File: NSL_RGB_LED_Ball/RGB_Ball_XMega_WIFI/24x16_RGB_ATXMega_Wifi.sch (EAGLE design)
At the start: 105 parts, among them IC2 TLC5947XLP, IC3 TLC5947XLP, IC4 TLC5947XLP, IC5 MCP73123, IC6 CC3000, IC7 MMA7455L, IC8 OPA344, X1 NX3225GA XC1972CT-ND

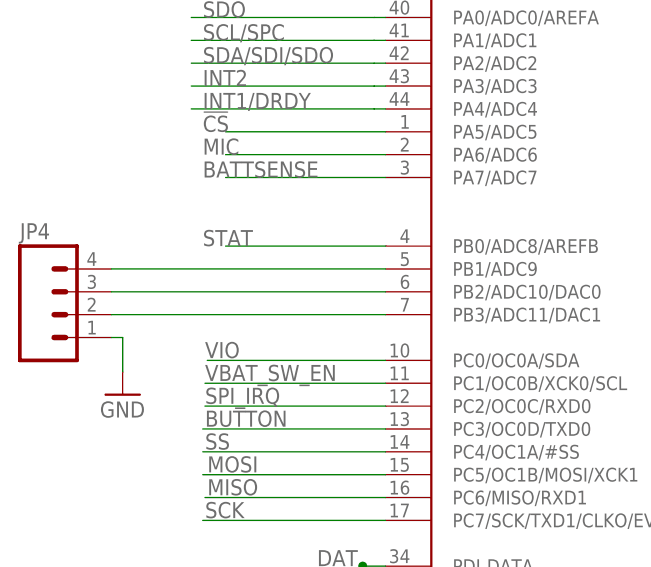
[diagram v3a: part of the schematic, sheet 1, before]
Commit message: 
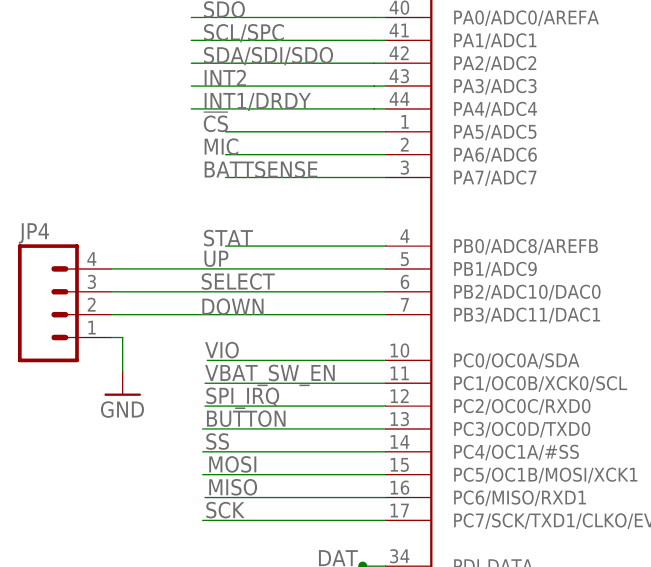
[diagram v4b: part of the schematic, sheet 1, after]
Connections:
- net N$18 renamed DOWN
- net N$4 renamed UP
- net N$5 renamed SELECT
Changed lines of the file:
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@@
 </segment>
 </net>
-<net name="N$4" class="0">
+<net name="UP" class="0">
 <segment>
 <pinref part="IC1" gate="G$1" pin="PB1/ADC9"/>
 <wire x1="-40.64" y1="-44.45" x2="-71.12" y2="-44.45" width="0.1524" layer="91"/>
 <pinref part="JP4" gate="G$1" pin="4"/>
+<label x="-60.96" y="-44.196" size="1.778" layer="95"/>
 </segment>
 </net>
-<net name="N$5" class="0">
+<net name="SELECT" class="0">
 <segment>
 <pinref part="IC1" gate="G$1" pin="PB2/ADC10/DAC0"/>
 <wire x1="-40.64" y1="-46.99" x2="-71.12" y2="-46.99" width="0.1524" layer="91"/>
 <pinref part="JP4" gate="G$1" pin="3"/>
+<label x="-61.214" y="-46.736" size="1.778" layer="95"/>
 </segment>
 </net>
-<net name="N$18" class="0">
+<net name="DOWN" class="0">
 <segment>
 <pinref part="IC1" gate="G$1" pin="PB3/ADC11/DAC1"/>
 <wire x1="-40.64" y1="-49.53" x2="-71.12" y2="-49.53" width="0.1524" layer="91"/>
 <pinref part="JP4" gate="G$1" pin="2"/>
+<label x="-61.214" y="-49.53" size="1.778" layer="95"/>
 </segment>
 </net>

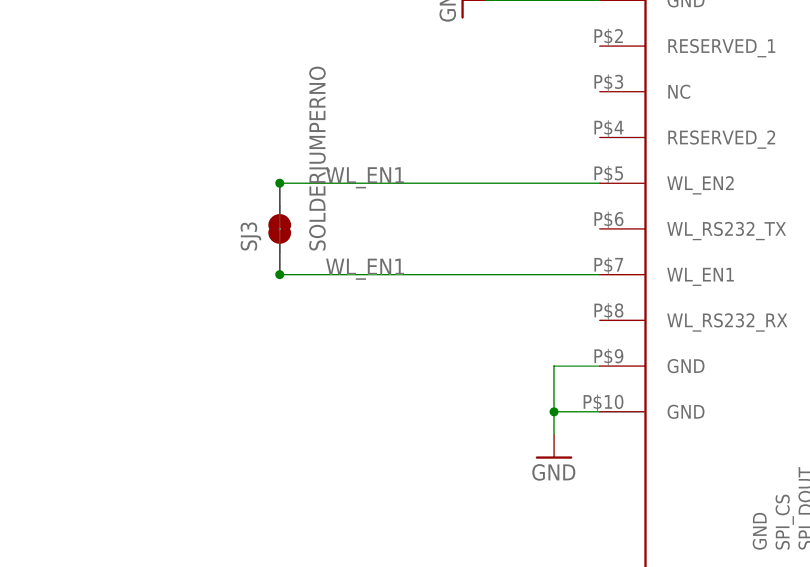
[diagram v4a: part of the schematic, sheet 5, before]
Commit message: 
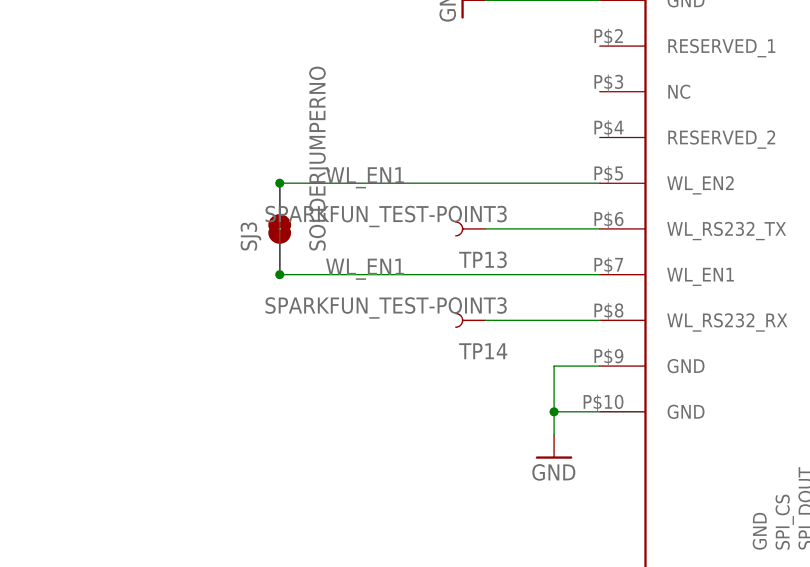
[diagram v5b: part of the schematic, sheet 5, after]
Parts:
- added TP13, TP14: SPARKFUN_TEST-POINT3, badge.lbrbadge_2013:SPARKFUN_TEST-POINT3
- X1: value NX3225GA XC1972CT-ND -> NX3225GA-16.000M-STD-CRG-2; device M6-RF315:NX3225GA -> 24x16_RGB_ATXMega_Wifi:NX3225GA
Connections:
- new net N$21: IC6.WL_RS232_TX, TP13.1
- new net N$23: IC6.WL_RS232_RX, TP14.1
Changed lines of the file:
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@@
 <part name="C8" library="SparkFun" deviceset="CAP" device="0805" value="0.1uF"/>
 <part name="GND23" library="SparkFun" deviceset="GND" device=""/>
-<part name="X1" library="M6-RF315" deviceset="NX3225GA" device="" value="NX3225GA XC1972CT-ND"/>
+<part name="X1" library="24x16_RGB_ATXMega_Wifi" deviceset="NX3225GA" device="" value="NX3225GA-16.000M-STD-CRG-2"/>
 <part name="C4" library="SparkFun" deviceset="CAP" device="0805" value="10pF"/>
 <part name="C3" library="SparkFun" deviceset="CAP" device="0805" value="10pF"/>
@@
 <part name="GND32" library="SparkFun" deviceset="GND" device=""/>
 <part name="SUPPLY4" library="supply2" deviceset="VCC" device=""/>
+<part name="TP13" library="badge.lbrbadge_2013" deviceset="SPARKFUN_TEST-POINT" device="3"/>
+<part name="TP14" library="badge.lbrbadge_2013" deviceset="SPARKFUN_TEST-POINT" device="3"/>
 </parts>
 <sheets>
@@
 </instance>
 <instance part="GND19" gate="1" x="17.78" y="-96.52"/>
+<instance part="TP13" gate="G$1" x="-109.22" y="-81.28" rot="R180"/>
+<instance part="TP14" gate="G$1" x="-109.22" y="-91.44" rot="R180"/>
 </instances>
 <busses>
@@
 </segment>
 </net>
+<net name="N$21" class="0">
+<segment>
+<pinref part="TP13" gate="G$1" pin="1"/>
+<pinref part="IC6" gate="G$1" pin="WL_RS232_TX"/>
+<wire x1="-109.22" y1="-81.28" x2="-96.52" y2="-81.28" width="0.1524" layer="91"/>
+</segment>
+</net>
+<net name="N$23" class="0">
+<segment>
+<pinref part="TP14" gate="G$1" pin="1"/>
+<pinref part="IC6" gate="G$1" pin="WL_RS232_RX"/>
+<wire x1="-109.22" y1="-91.44" x2="-96.52" y2="-91.44" width="0.1524" layer="91"/>
+</segment>
+</net>

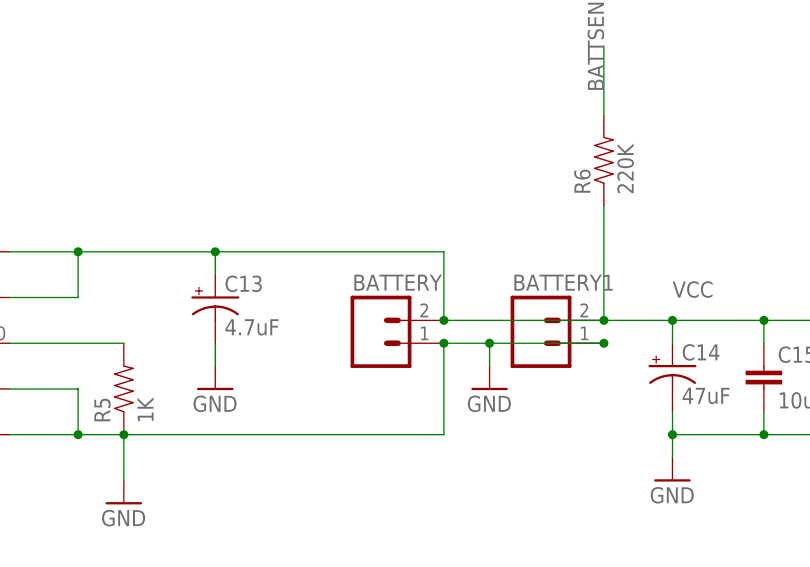
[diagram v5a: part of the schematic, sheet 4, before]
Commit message: 
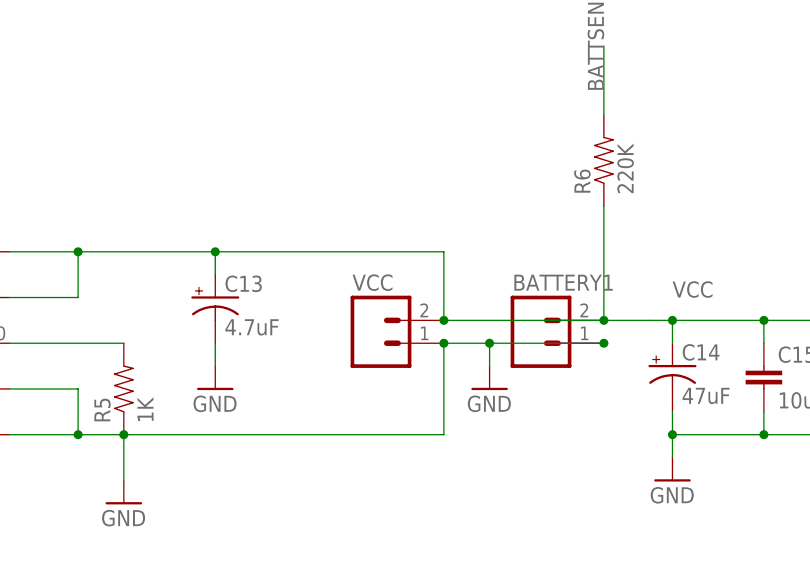
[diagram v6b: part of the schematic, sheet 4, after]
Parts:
- renumbered BATTERY to VCC
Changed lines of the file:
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@@
 <attribute name="OC_NEWARK" value="unknown"/>
 </part>
-<part name="BATTERY" library="SparkFun" deviceset="M02" device="PTH">
+<part name="VCC" library="SparkFun" deviceset="M02" device="PTH">
 <attribute name="MF" value=""/>
 <attribute name="MPN" value=""/>
@@
 </plain>
 <instances>
-<instance part="BATTERY" gate="G$1" x="60.96" y="-2.54">
+<instance part="VCC" gate="G$1" x="60.96" y="-2.54">
 <attribute name="OC_NEWARK" x="60.96" y="-2.54" size="1.778" layer="96" display="off"/>
 <attribute name="MF" x="60.96" y="-2.54" size="1.778" layer="96" display="off"/>
@@
 <pinref part="R5" gate="G$1" pin="1"/>
 <pinref part="GND8" gate="1" pin="GND"/>
-<pinref part="BATTERY" gate="G$1" pin="1"/>
+<pinref part="VCC" gate="G$1" pin="1"/>
 <pinref part="GND2" gate="1" pin="GND"/>
 <pinref part="BATTERY1" gate="G$1" pin="1"/>
@@
 <junction x="68.58" y="0"/>
 <junction x="43.18" y="7.62"/>
-<pinref part="BATTERY" gate="G$1" pin="2"/>
+<pinref part="VCC" gate="G$1" pin="2"/>
 <pinref part="IC5" gate="G$1" pin="VBAT@1"/>
 <pinref part="IC5" gate="G$1" pin="VBAT@2"/>

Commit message: 
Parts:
- R1, R2, R3: value 20K -> 24K
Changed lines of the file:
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@@
 <attribute name="OC_NEWARK" value="unknown"/>
 </part>
-<part name="R1" library="24x16_RGB" deviceset="RESISTOR" device="" value="20K">
+<part name="R1" library="24x16_RGB" deviceset="RESISTOR" device="" value="24K">
 <attribute name="MF" value=""/>
 <attribute name="MPN" value=""/>
@@
 <attribute name="OC_NEWARK" value="unknown"/>
 </part>
-<part name="R2" library="24x16_RGB" deviceset="RESISTOR" device="" value="20K">
+<part name="R2" library="24x16_RGB" deviceset="RESISTOR" device="" value="24K">
 <attribute name="MF" value=""/>
 <attribute name="MPN" value=""/>
@@
 <attribute name="OC_NEWARK" value="unknown"/>
 </part>
-<part name="R3" library="24x16_RGB" deviceset="RESISTOR" device="" value="20K">
+<part name="R3" library="24x16_RGB" deviceset="RESISTOR" device="" value="24K">
 <attribute name="MF" value=""/>
 <attribute name="MPN" value=""/>

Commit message: 
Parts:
- R1, R2, R3: value 24K -> 47K
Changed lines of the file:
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@@
 <attribute name="OC_NEWARK" value="unknown"/>
 </part>
-<part name="R1" library="24x16_RGB" deviceset="RESISTOR" device="" value="24K">
+<part name="R1" library="24x16_RGB" deviceset="RESISTOR" device="" value="47K">
 <attribute name="MF" value=""/>
 <attribute name="MPN" value=""/>
@@
 <attribute name="OC_NEWARK" value="unknown"/>
 </part>
-<part name="R2" library="24x16_RGB" deviceset="RESISTOR" device="" value="24K">
+<part name="R2" library="24x16_RGB" deviceset="RESISTOR" device="" value="47K">
 <attribute name="MF" value=""/>
 <attribute name="MPN" value=""/>
@@
 <attribute name="OC_NEWARK" value="unknown"/>
 </part>
-<part name="R3" library="24x16_RGB" deviceset="RESISTOR" device="" value="24K">
+<part name="R3" library="24x16_RGB" deviceset="RESISTOR" device="" value="47K">
 <attribute name="MF" value=""/>
 <attribute name="MPN" value=""/>
